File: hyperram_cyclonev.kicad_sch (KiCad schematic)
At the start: 57 parts, among them IC1 AP63205WU, IC2 TXB0108PWR, IC3 S26KL128SDABHI020, IC4 W25Q32JVSSIQ_TR, IC5 S27KL0641DABHI020, J1 ASP-122952-01, J2 HDMI_A, J3 Conn_02x10_Odd_Even, J4 Conn_02x06_Odd_Even, J5 Conn_02x06_Top_Bottom, J6 Conn_02x06_Top_Bottom, J7 Conn_02x06_Top_Bottom, Q1 BSS138, Q2 BSS138

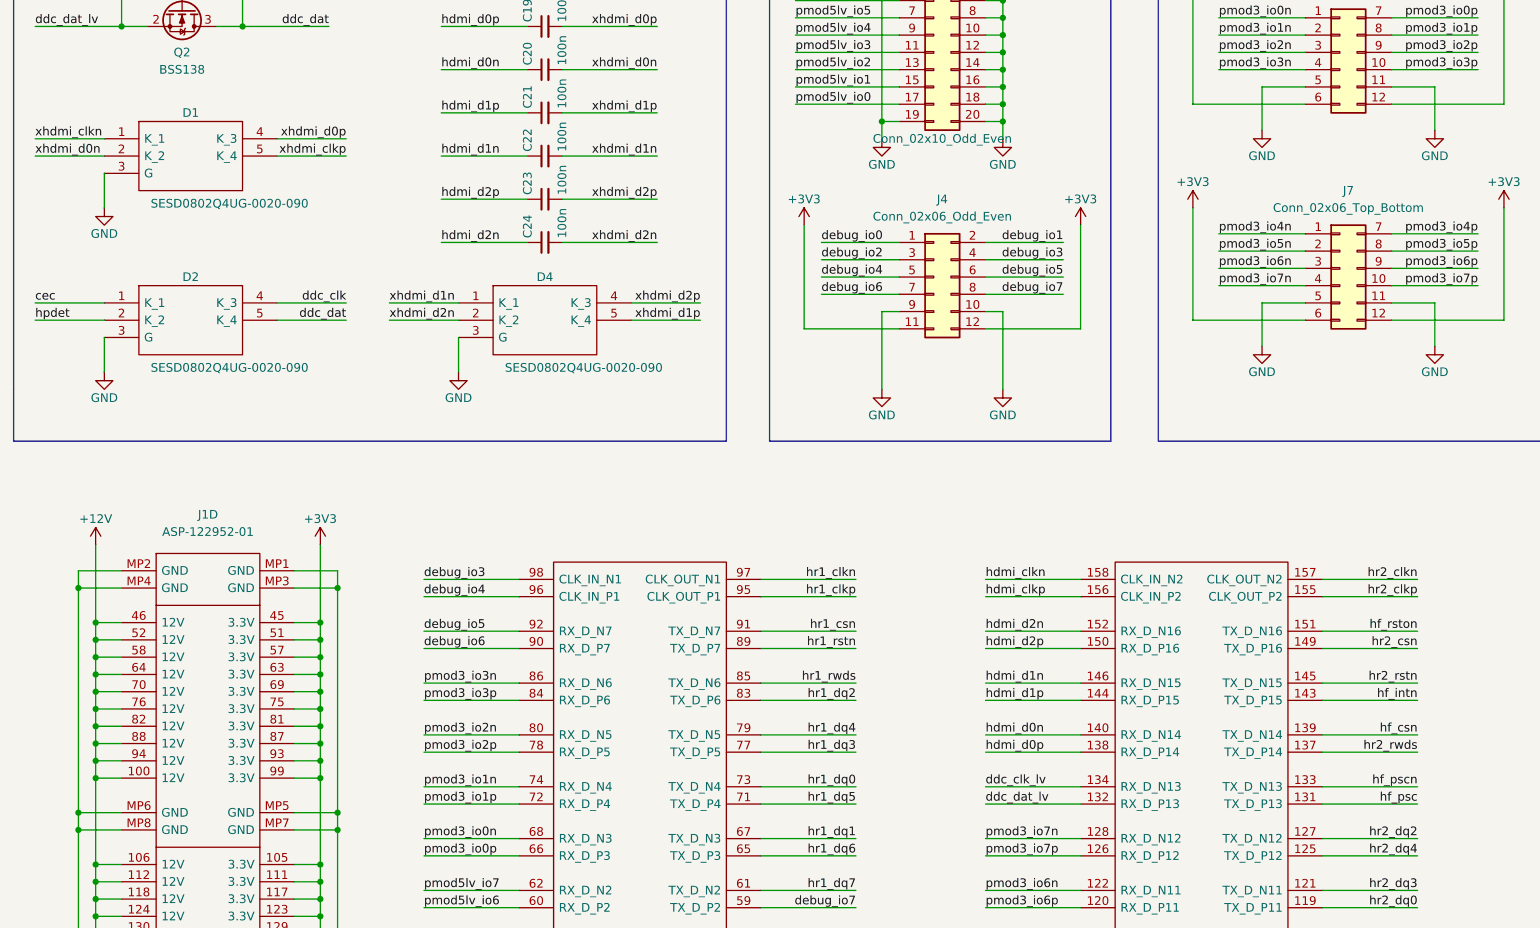
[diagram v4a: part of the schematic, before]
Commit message: Optimizing signal assigments and component placement to simplify routing.
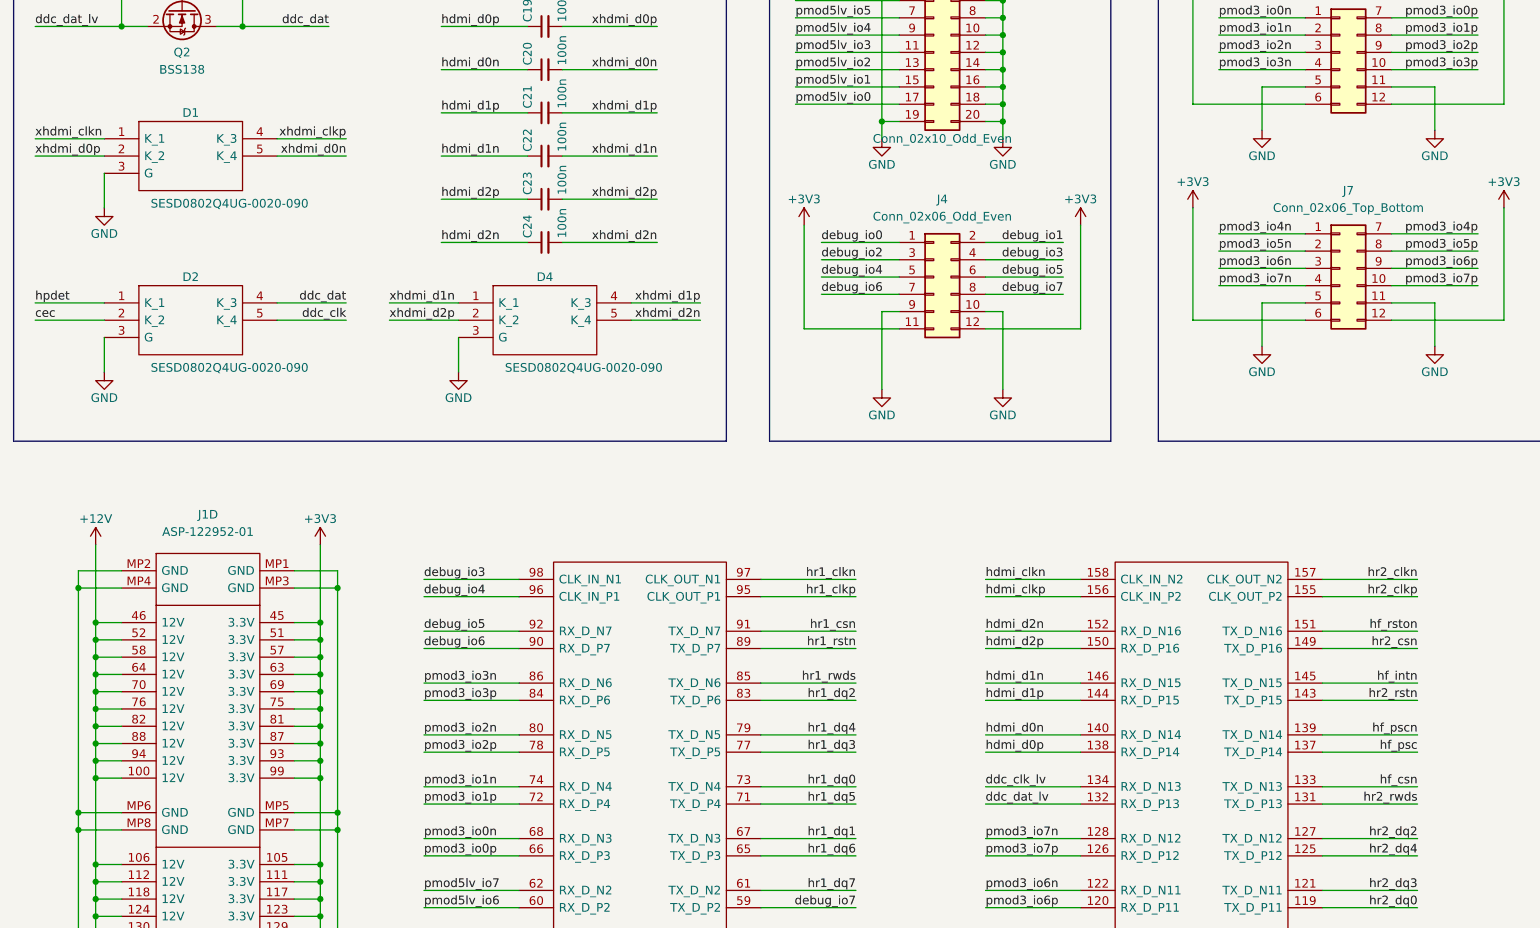
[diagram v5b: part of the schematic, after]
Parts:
- C17, C18, C19, C20, C21, C22, C23, C24: footprint Capacitor_SMD:C_0603_1608Metric_Pad1.08x0.95mm_HandSolder -> Capacitor_SMD:C_0402_1005Metric_Pad0.74x0.62mm_HandSolder
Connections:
- net cec: now also D2.2 (K_2); no longer D2.1 (K_1)
- net ddc_clk: now also D2.5 (K_4); no longer D2.4 (K_3)
- net ddc_dat: now also D2.4 (K_3); no longer D2.5 (K_4)
- net hf_csn: now also J1.133 (TX_D_N13); no longer J1.139 (TX_D_N14)
- net hf_intn: now also J1.145 (TX_D_N15); no longer J1.143 (TX_D_P15)
- net hf_psc: now also J1.137 (TX_D_P14); no longer J1.131 (TX_D_P13)
- net hf_pscn: now also J1.139 (TX_D_N14); no longer J1.133 (TX_D_N13)
- net hpdet: now also D2.1 (K_1); no longer D2.2 (K_2)
- net hr2_rstn: now also J1.143 (TX_D_P15); no longer J1.145 (TX_D_N15)
- net hr2_rwds: now also J1.131 (TX_D_P13); no longer J1.137 (TX_D_P14)
- net xhdmi_clkp: now also D1.4 (K_3); no longer D1.5 (K_4)
- net xhdmi_d0n: now also D1.5 (K_4); no longer D1.2 (K_2)
- net xhdmi_d0p: now also D1.2 (K_2); no longer D1.4 (K_3)
- net xhdmi_d1p: now also D4.4 (K_3); no longer D4.5 (K_4)
- net xhdmi_d2n: now also D4.5 (K_4); no longer D4.2 (K_2)
- net xhdmi_d2p: now also D4.2 (K_2); no longer D4.4 (K_3)
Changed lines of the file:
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@@
 	)
 	(label "ddc_dat"
-		(at 64.77 154.94 180)
+		(at 64.77 152.4 180)
 		(fields_autoplaced yes)
 		(effects
@@
 	)
 	(label "ddc_clk"
-		(at 64.77 152.4 180)
+		(at 64.77 154.94 180)
 		(fields_autoplaced yes)
 		(effects
@@
 	)
 	(label "hpdet"
-		(at 19.05 154.94 0)
+		(at 19.05 152.4 0)
 		(fields_autoplaced yes)
 		(effects
@@
 	)
 	(label "xhdmi_d2p"
-		(at 116.84 152.4 180)
+		(at 71.12 154.94 0)
 		(fields_autoplaced yes)
 		(effects
@@
 				(size 1.27 1.27)
 			)
-			(justify right bottom)
+			(justify left bottom)
 		)
 	)
@@
 	)
 	(label "xhdmi_d0n"
-		(at 19.05 130.81 0)
+		(at 64.77 130.81 180)
 		(fields_autoplaced yes)
 		(effects
@@
 				(size 1.27 1.27)
 			)
-			(justify left bottom)
+			(justify right bottom)
 		)
 	)
@@
 	)
 	(label "xhdmi_d1p"
-		(at 116.84 154.94 180)
+		(at 116.84 152.4 180)
 		(fields_autoplaced yes)
 		(effects
@@
 	)
 	(label "hf_pscn"
-		(at 222.25 223.52 180)
+		(at 222.25 215.9 180)
 		(fields_autoplaced yes)
 		(effects
@@
 	)
 	(label "hr2_rstn"
-		(at 222.25 208.28 180)
+		(at 222.25 210.82 180)
 		(fields_autoplaced yes)
 		(effects
@@
 	)
 	(label "hr2_rwds"
-		(at 222.25 218.44 180)
+		(at 222.25 226.06 180)
 		(fields_autoplaced yes)
 		(effects
@@
 	)
 	(label "hf_intn"
-		(at 222.25 210.82 180)
+		(at 222.25 208.28 180)
 		(fields_autoplaced yes)
 		(effects
@@
 	)
 	(label "cec"
-		(at 19.05 152.4 0)
+		(at 19.05 154.94 0)
 		(fields_autoplaced yes)
 		(effects
@@
 	)
 	(label "hf_csn"
-		(at 222.25 215.9 180)
+		(at 222.25 223.52 180)
 		(fields_autoplaced yes)
 		(effects
@@
 	)
 	(label "hf_psc"
-		(at 222.25 226.06 180)
+		(at 222.25 218.44 180)
 		(fields_autoplaced yes)
 		(effects
@@
 	)
 	(label "xhdmi_d2n"
-		(at 71.12 154.94 0)
+		(at 116.84 154.94 180)
 		(fields_autoplaced yes)
 		(effects
@@
 				(size 1.27 1.27)
 			)
-			(justify left bottom)
+			(justify right bottom)
 		)
 	)
@@
 	)
 	(label "xhdmi_clkp"
-		(at 64.77 130.81 180)
+		(at 64.77 128.27 180)
 		(fields_autoplaced yes)
 		(effects
@@
 	)
 	(label "xhdmi_d0p"
-		(at 64.77 128.27 180)
+		(at 19.05 130.81 0)
 		(fields_autoplaced yes)
 		(effects
@@
 				(size 1.27 1.27)
 			)
-			(justify right bottom)
+			(justify left bottom)
 		)
 	)
@@
 			)
 		)
-		(property "Footprint" "Capacitor_SMD:C_0603_1608Metric_Pad1.08x0.95mm_HandSolder"
+		(property "Footprint" "Capacitor_SMD:C_0402_1005Metric_Pad0.74x0.62mm_HandSolder"
 			(at 93.98 124.46 0)
 			(effects
@@
 			)
 		)
-		(property "Footprint" "Capacitor_SMD:C_0603_1608Metric_Pad1.08x0.95mm_HandSolder"
+		(property "Footprint" "Capacitor_SMD:C_0402_1005Metric_Pad0.74x0.62mm_HandSolder"
 			(at 93.98 118.11 0)
 			(effects
@@
 			)
 		)
-		(property "Footprint" "Capacitor_SMD:C_0603_1608Metric_Pad1.08x0.95mm_HandSolder"
+		(property "Footprint" "Capacitor_SMD:C_0402_1005Metric_Pad0.74x0.62mm_HandSolder"
 			(at 93.98 105.41 0)
 			(effects
@@
 			)
 		)
-		(property "Footprint" "Capacitor_SMD:C_0603_1608Metric_Pad1.08x0.95mm_HandSolder"
+		(property "Footprint" "Capacitor_SMD:C_0402_1005Metric_Pad0.74x0.62mm_HandSolder"
 			(at 93.98 99.06 0)
 			(effects
@@
 			)
 		)
-		(property "Footprint" "Capacitor_SMD:C_0603_1608Metric_Pad1.08x0.95mm_HandSolder"
+		(property "Footprint" "Capacitor_SMD:C_0402_1005Metric_Pad0.74x0.62mm_HandSolder"
 			(at 93.98 143.51 0)
 			(effects
@@
 			)
 		)
-		(property "Footprint" "Capacitor_SMD:C_0603_1608Metric_Pad1.08x0.95mm_HandSolder"
+		(property "Footprint" "Capacitor_SMD:C_0402_1005Metric_Pad0.74x0.62mm_HandSolder"
 			(at 93.98 111.76 0)
 			(effects
@@
 			)
 		)
-		(property "Footprint" "Capacitor_SMD:C_0603_1608Metric_Pad1.08x0.95mm_HandSolder"
+		(property "Footprint" "Capacitor_SMD:C_0402_1005Metric_Pad0.74x0.62mm_HandSolder"
 			(at 93.98 130.81 0)
 			(effects
@@
 			)
 		)
-		(property "Footprint" "Capacitor_SMD:C_0603_1608Metric_Pad1.08x0.95mm_HandSolder"
+		(property "Footprint" "Capacitor_SMD:C_0402_1005Metric_Pad0.74x0.62mm_HandSolder"
 			(at 93.98 137.16 0)
 			(effects

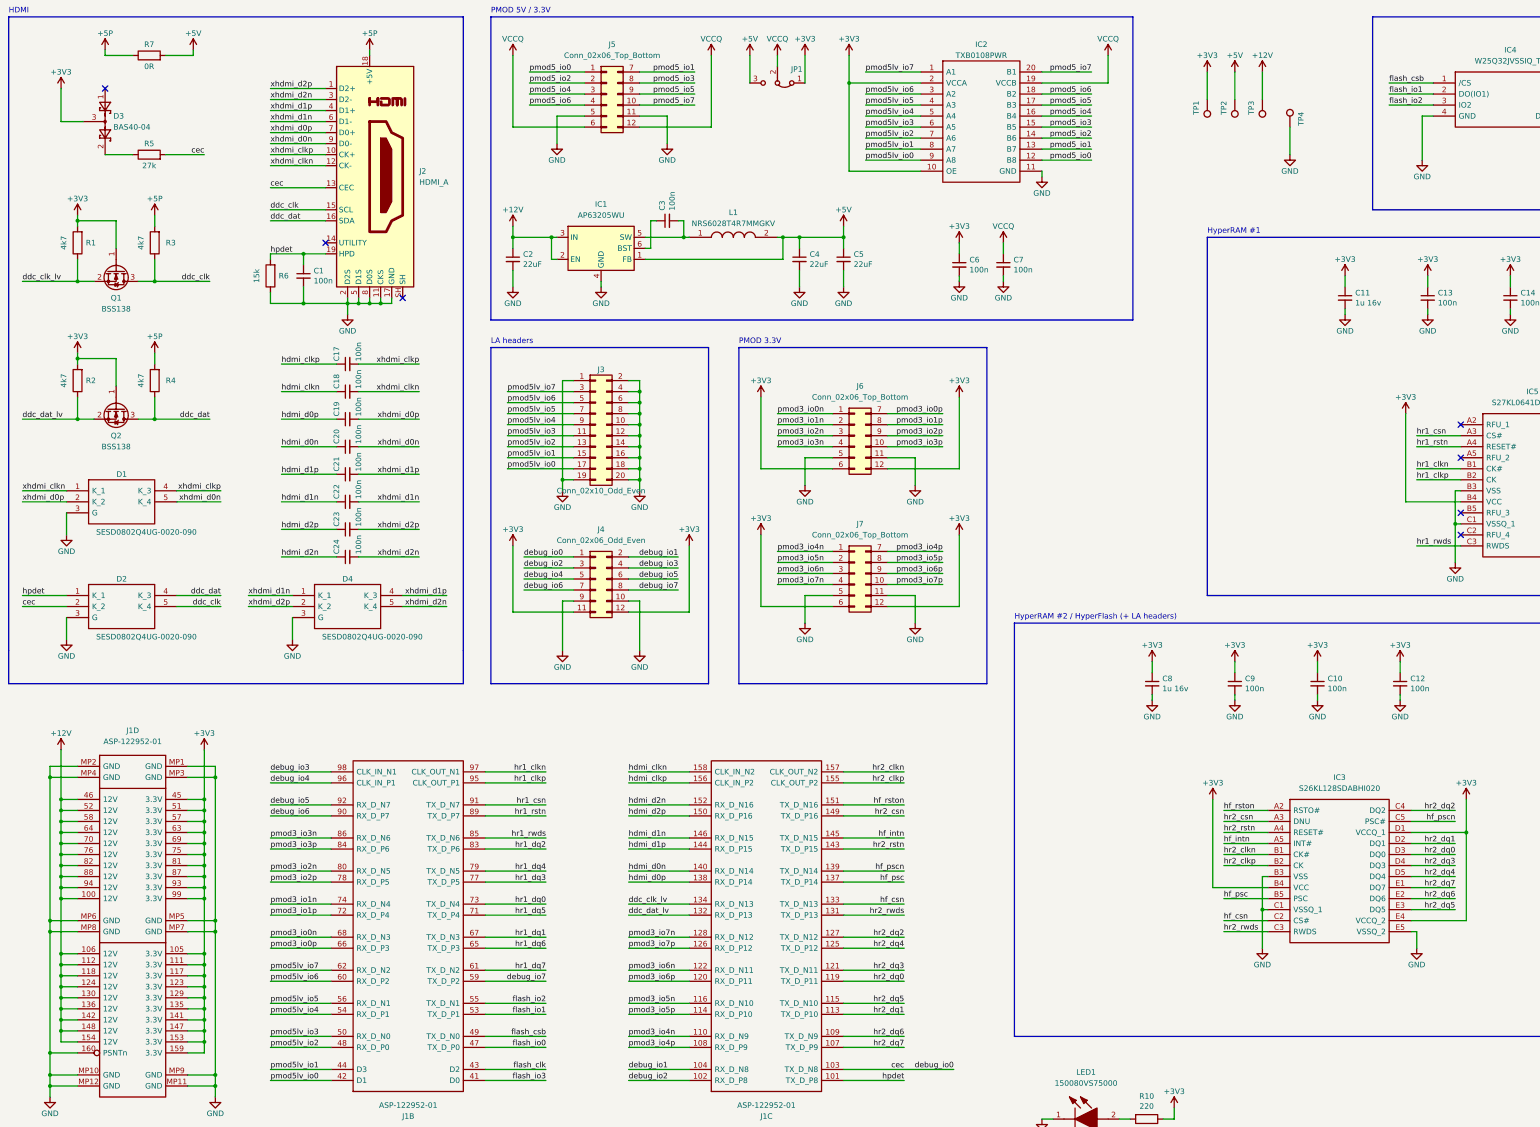
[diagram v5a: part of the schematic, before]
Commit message: Fixed differential pairs designators for HyperRAM clk and psc and HDMI clk and data.
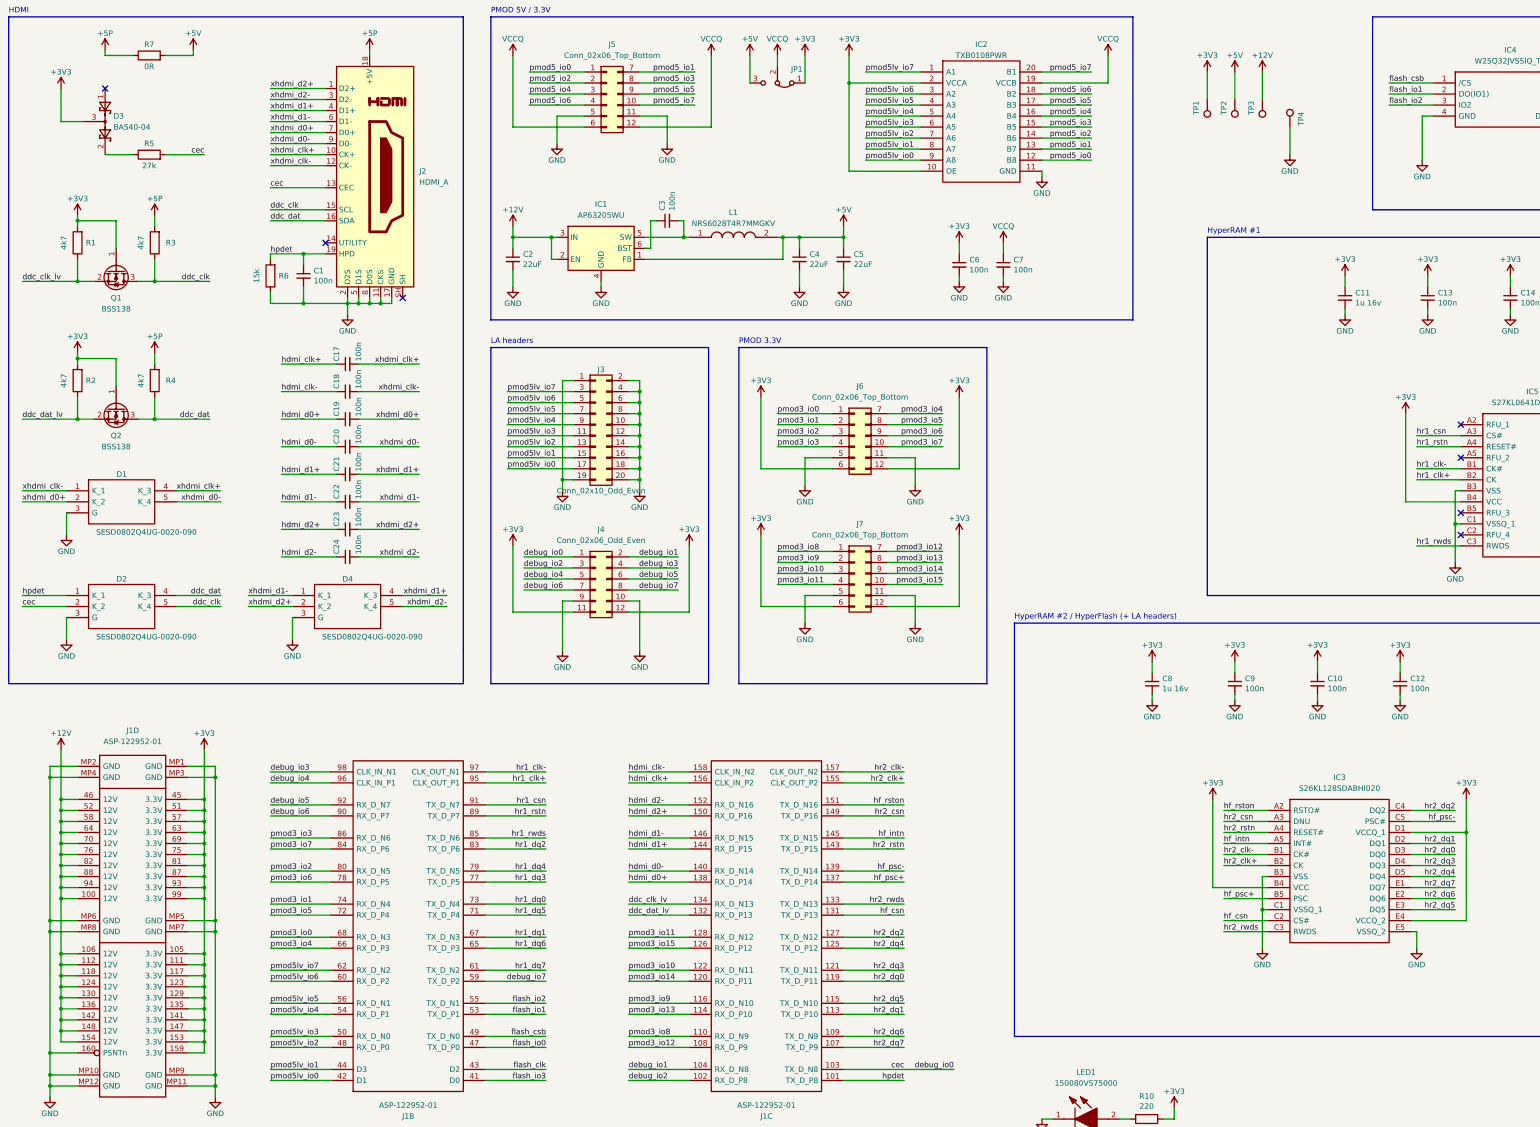
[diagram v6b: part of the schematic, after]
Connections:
- net hf_csn: now also J1.131 (TX_D_P13); no longer J1.133 (TX_D_N13)
- net hr2_rwds: now also J1.133 (TX_D_N13); no longer J1.131 (TX_D_P13)
- net hdmi_clkn renamed hdmi_clk-
- net hdmi_clkp renamed hdmi_clk+
- net hdmi_d0n renamed hdmi_d0-
- net hdmi_d0p renamed hdmi_d0+
- net hdmi_d1n renamed hdmi_d1-
- net hdmi_d1p renamed hdmi_d1+
- net hdmi_d2n renamed hdmi_d2-
- net hdmi_d2p renamed hdmi_d2+
- net hf_psc renamed hf_psc+
- net hf_pscn renamed hf_psc-
- net hr1_clkn renamed hr1_clk-
- net hr1_clkp renamed hr1_clk+
- net hr2_clkn renamed hr2_clk-
- net hr2_clkp renamed hr2_clk+
- net pmod3_io0n renamed pmod3_io0
- net pmod3_io0p renamed pmod3_io4
- net pmod3_io1n renamed pmod3_io1
- net pmod3_io1p renamed pmod3_io5
- net pmod3_io2n renamed pmod3_io2
- net pmod3_io2p renamed pmod3_io6
- net pmod3_io3n renamed pmod3_io3
- net pmod3_io3p renamed pmod3_io7
- net pmod3_io4n renamed pmod3_io8
- net pmod3_io4p renamed pmod3_io12
- net pmod3_io5n renamed pmod3_io9
- net pmod3_io5p renamed pmod3_io13
- net pmod3_io6n renamed pmod3_io10
- net pmod3_io6p renamed pmod3_io14
- net pmod3_io7n renamed pmod3_io11
- net pmod3_io7p renamed pmod3_io15
- net xhdmi_clkn renamed xhdmi_clk-
- net xhdmi_clkp renamed xhdmi_clk+
- net xhdmi_d0n renamed xhdmi_d0-
- net xhdmi_d0p renamed xhdmi_d0+
- net xhdmi_d1n renamed xhdmi_d1-
- net xhdmi_d1p renamed xhdmi_d1+
- net xhdmi_d2n renamed xhdmi_d2-
- net xhdmi_d2p renamed xhdmi_d2+
